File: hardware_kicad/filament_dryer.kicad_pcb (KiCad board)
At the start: 2 copper layers, 94 x 130 mm, 98 parts, among them J1 USB_C_Receptacle_USB2.0, J2 H/T Ambient, J3 T Aux, J4 Peristaltic Pump, Q1 NMOS, Q2 NMOS, Q3 NMOS, Q4 NMOS, U1 W25Q128JVS, U2 AMS1117-3.3, U3 RP2040, U4 DS18B20Z, U5 H/T Filament, X1 12MHz Yangxing Tech X322512MS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

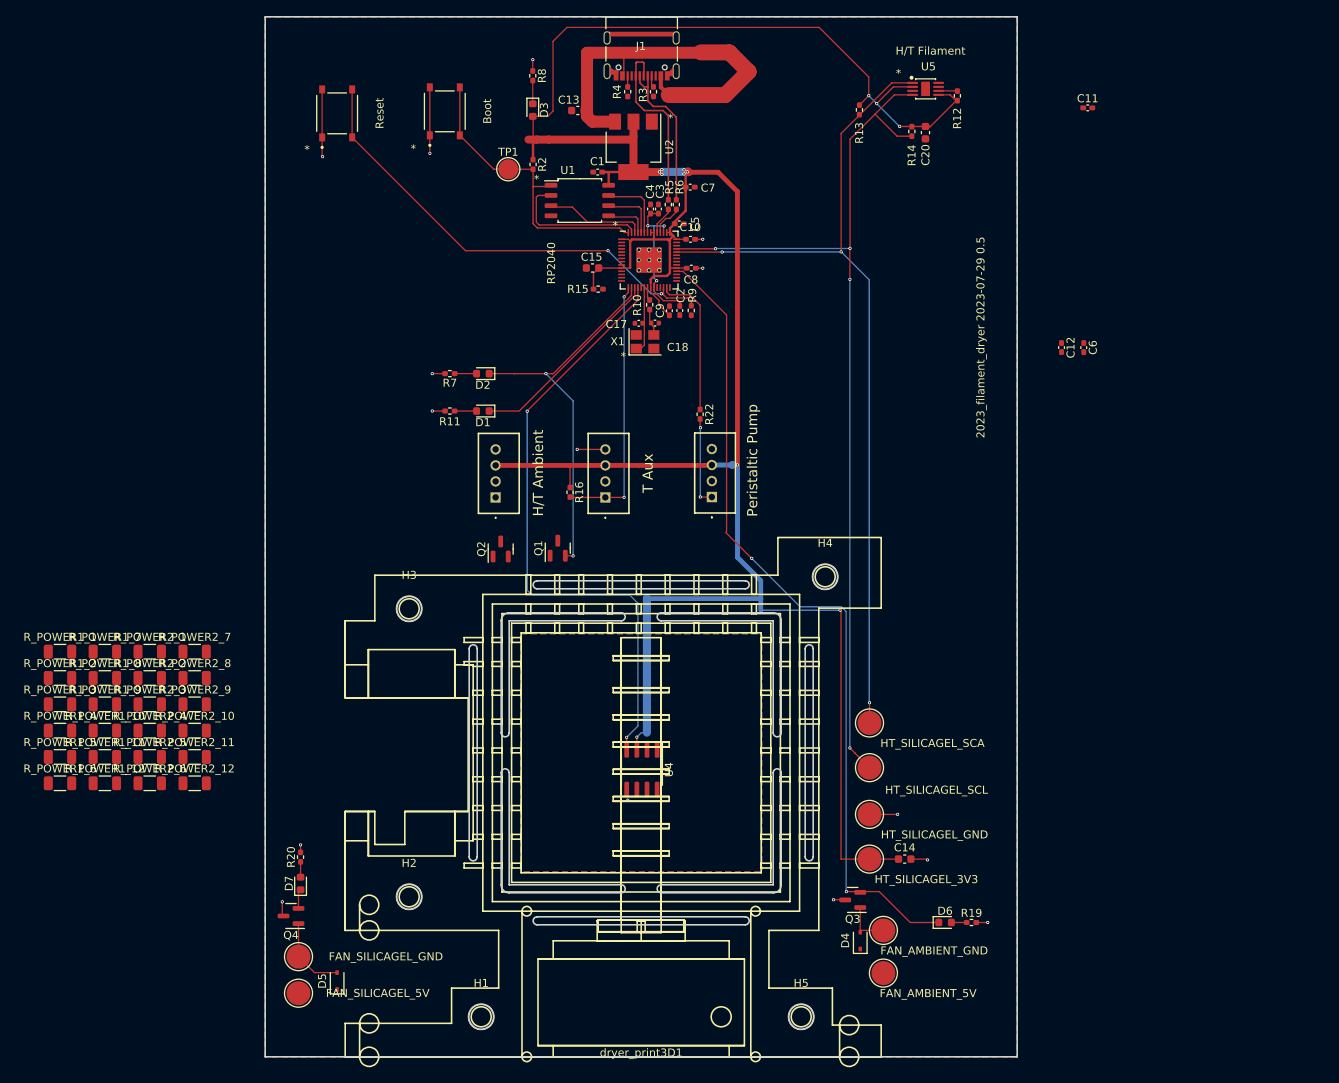
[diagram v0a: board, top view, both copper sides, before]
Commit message: Last version with resistors
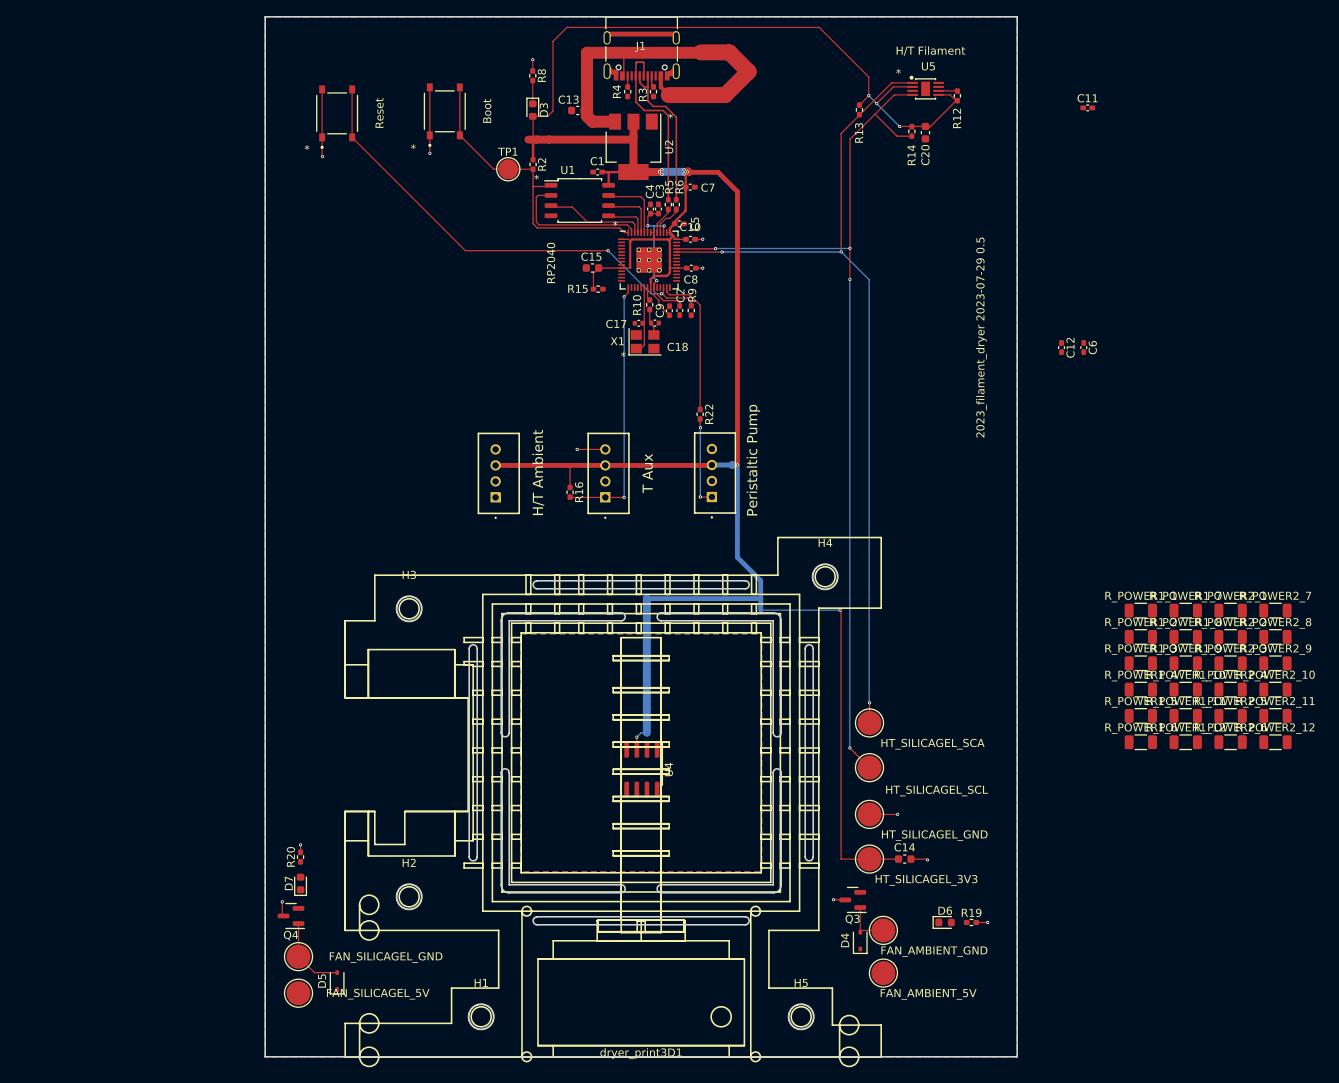
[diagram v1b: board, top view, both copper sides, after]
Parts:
- removed D1: HEATER_2, LED_SMD:LED_0603_1608Metric
- removed D2: HEATER_1, LED_SMD:LED_0603_1608Metric
- removed Q1, Q2: NMOS, Package_TO_SOT_SMD:SOT-23
- removed R11, R7: 470R, Resistor_SMD:R_0402_1005Metric_Pad0.72x0.64mm_HandSolder
- moved R_POWER1_1 135.2 mm to (163.5, 114.2)
- moved R_POWER1_10 135.2 mm to (169.1, 124.1)
- moved R_POWER1_11 135.2 mm to (169.1, 127.4)
- moved R_POWER1_12 135.2 mm to (169.1, 130.7)
- moved R_POWER1_2 135.2 mm to (163.5, 117.5)
- moved R_POWER1_3 135.2 mm to (163.5, 120.8)
- moved R_POWER1_4 135.2 mm to (163.5, 124.1)
- moved R_POWER1_5 135.2 mm to (163.5, 127.4)
- moved R_POWER1_6 135.2 mm to (163.5, 130.7)
- moved R_POWER1_7 135.2 mm to (169.1, 114.2)
- moved R_POWER1_8 135.2 mm to (169.1, 117.5)
- moved R_POWER1_9 135.2 mm to (169.1, 120.8)
- moved R_POWER2_1 135.2 mm to (174.7, 114.2)
- moved R_POWER2_10 135.2 mm to (180.3, 124.1)
- moved R_POWER2_11 135.2 mm to (180.3, 127.4)
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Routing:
- net /GPIO_FAN_AMBIENT: track 104.9 -> 0.00 mm, vias 2 -> 0
- net /T_HEATING_1WIRE: track 77.0 -> 0.00 mm, vias 2 -> 0
- net /GPIO_HEATER_1: track 48.0 -> 0.00 mm, vias 2 -> 0
- net /GPIO_HEATER_2: track 25.1 -> 0.00 mm
- net +5V: track 54.6 -> 49.1 mm
- net /GPIO_FAN_SILICAGEL: track 3.99 -> 0.00 mm
- net Net-(Q2-D): track 1.60 -> 0.00 mm, vias 1 -> 0
- net Net-(Q1-D): track 1.60 -> 0.00 mm, vias 1 -> 0
- net GND: vias 13 -> 12

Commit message: Ready for second review
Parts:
- removed R_POWER1_1, R_POWER1_10, R_POWER1_11, R_POWER1_12, R_POWER1_2, R_POWER1_3, R_POWER1_4, R_POWER1_5, R_POWER1_6, R_POWER1_7, R_POWER1_8, R_POWER1_9, R_POWER2_1, R_POWER2_10, R_POWER2_11, R_POWER2_12, R_POWER2_2, R_POWER2_3, R_POWER2_4, R_POWER2_5, R_POWER2_6, R_POWER2_7, R_POWER2_8, R_POWER2_9: 120, Resistor_SMD:R_1206_3216Metric
- added D10: 1N4148WS, Diode_SMD:D_SOD-323, F.Cu at (84.7, 83.6)
- added D11: 1N4148WS, Diode_SMD:D_SOD-323, F.Cu at (62.7, 83.6)
- added D8: 1N4148WS, Diode_SMD:D_SOD-323, F.Cu at (75.2, 83.6)
- added D9: 1N4148WS, Diode_SMD:D_SOD-323, F.Cu at (136.9, 83.6)
- added JP1: SolderJumper_2_Open, Jumper:SolderJumper-2_P1.3mm_Open_RoundedPad1.0x1.5mm, F.Cu at (70.4, 81.1)
- added JP2: SolderJumper_2_Open, Jumper:SolderJumper-2_P1.3mm_Open_RoundedPad1.0x1.5mm, F.Cu at (132.0, 81.0)
- added JP3: SolderJumper_2_Open, Jumper:SolderJumper-2_P1.3mm_Open_RoundedPad1.0x1.5mm, F.Cu at (79.8, 81.1)
- added JP4: SolderJumper_2_Open, Jumper:SolderJumper-2_P1.3mm_Open_RoundedPad1.0x1.5mm, F.Cu at (57.8, 81.1)
- added NeoC1: 100n, Capacitor_SMD:C_0402_1005Metric_Pad0.74x0.62mm_HandSolder, F.Cu at (87.6, 119.5)
- added NeoC10: 100n, Capacitor_SMD:C_0402_1005Metric_Pad0.74x0.62mm_HandSolder, F.Cu at (87.6, 145.6)
- added NeoC11: 100n, Capacitor_SMD:C_0402_1005Metric_Pad0.74x0.62mm_HandSolder, F.Cu at (109.6, 119.5)
- added NeoC12: 100n, Capacitor_SMD:C_0402_1005Metric_Pad0.74x0.62mm_HandSolder, F.Cu at (109.6, 122.4)
- added NeoC13: 100n, Capacitor_SMD:C_0402_1005Metric_Pad0.74x0.62mm_HandSolder, F.Cu at (109.6, 125.3)
- added NeoC14: 100n, Capacitor_SMD:C_0402_1005Metric_Pad0.74x0.62mm_HandSolder, F.Cu at (109.6, 128.2)
- added NeoC15: 100n, Capacitor_SMD:C_0402_1005Metric_Pad0.74x0.62mm_HandSolder, F.Cu at (109.6, 131.1)
- added NeoC16: 100n, Capacitor_SMD:C_0402_1005Metric_Pad0.74x0.62mm_HandSolder, F.Cu at (109.6, 134.0)
- added NeoC17: 100n, Capacitor_SMD:C_0402_1005Metric_Pad0.74x0.62mm_HandSolder, F.Cu at (109.6, 136.9)
- added NeoC18: 100n, Capacitor_SMD:C_0402_1005Metric_Pad0.74x0.62mm_HandSolder, F.Cu at (109.6, 139.8)
- added NeoC19: 100n, Capacitor_SMD:C_0402_1005Metric_Pad0.74x0.62mm_HandSolder, F.Cu at (109.6, 142.7)
- added NeoC2: 100n, Capacitor_SMD:C_0402_1005Metric_Pad0.74x0.62mm_HandSolder, F.Cu at (87.6, 122.4)
- added NeoC20: 100n, Capacitor_SMD:C_0402_1005Metric_Pad0.74x0.62mm_HandSolder, F.Cu at (109.6, 145.6)
- added NeoC21: 100n, Capacitor_SMD:C_0402_1005Metric_Pad0.74x0.62mm_HandSolder, F.Cu at (97.6, 121.5)
- added NeoC22: 100n, Capacitor_SMD:C_0402_1005Metric_Pad0.74x0.62mm_HandSolder, F.Cu at (97.6, 124.4)
- added NeoC23: 100n, Capacitor_SMD:C_0402_1005Metric_Pad0.74x0.62mm_HandSolder, F.Cu at (97.6, 127.3)
- added NeoC24: 100n, Capacitor_SMD:C_0402_1005Metric_Pad0.74x0.62mm_HandSolder, F.Cu at (97.6, 140.0)
- added NeoC25: 100n, Capacitor_SMD:C_0402_1005Metric_Pad0.74x0.62mm_HandSolder, F.Cu at (97.6, 142.9)
- added NeoC26: 100n, Capacitor_SMD:C_0402_1005Metric_Pad0.74x0.62mm_HandSolder, F.Cu at (97.6, 145.8)
- added NeoC27: 100n, Capacitor_SMD:C_0402_1005Metric_Pad0.74x0.62mm_HandSolder, F.Cu at (58.2, 90.0)
- added NeoC28: 100n, Capacitor_SMD:C_0402_1005Metric_Pad0.74x0.62mm_HandSolder, F.Cu at (58.2, 94.5)
- added NeoC3: 100n, Capacitor_SMD:C_0402_1005Metric_Pad0.74x0.62mm_HandSolder, F.Cu at (87.6, 125.3)
- added NeoC4: 100n, Capacitor_SMD:C_0402_1005Metric_Pad0.74x0.62mm_HandSolder, F.Cu at (87.6, 128.2)
- added NeoC5: 100n, Capacitor_SMD:C_0402_1005Metric_Pad0.74x0.62mm_HandSolder, F.Cu at (87.6, 131.1)
- added NeoC6: 100n, Capacitor_SMD:C_0402_1005Metric_Pad0.74x0.62mm_HandSolder, F.Cu at (87.6, 134.0)
- added NeoC7: 100n, Capacitor_SMD:C_0402_1005Metric_Pad0.74x0.62mm_HandSolder, F.Cu at (87.6, 136.9)
- added NeoC8: 100n, Capacitor_SMD:C_0402_1005Metric_Pad0.74x0.62mm_HandSolder, F.Cu at (87.6, 139.8)
- added NeoC9: 100n, Capacitor_SMD:C_0402_1005Metric_Pad0.74x0.62mm_HandSolder, F.Cu at (87.6, 142.7)
- added NeoD1: WS2812B-2020, LED_SMD:LED_WS2812B-2020_PLCC4_2.0x2.0mm, F.Cu at (91.0, 119.0)
- added NeoD10: WS2812B-2020, LED_SMD:LED_WS2812B-2020_PLCC4_2.0x2.0mm, F.Cu at (91.0, 145.1)
- added NeoD11: WS2812B-2020, LED_SMD:LED_WS2812B-2020_PLCC4_2.0x2.0mm, F.Cu at (113.0, 119.0)
- added NeoD12: WS2812B-2020, LED_SMD:LED_WS2812B-2020_PLCC4_2.0x2.0mm, F.Cu at (113.0, 121.9)
- added NeoD13: WS2812B-2020, LED_SMD:LED_WS2812B-2020_PLCC4_2.0x2.0mm, F.Cu at (113.0, 124.8)
- added NeoD14: WS2812B-2020, LED_SMD:LED_WS2812B-2020_PLCC4_2.0x2.0mm, F.Cu at (113.0, 127.7)
- added NeoD15: WS2812B-2020, LED_SMD:LED_WS2812B-2020_PLCC4_2.0x2.0mm, F.Cu at (113.0, 130.6)
- added NeoD16: WS2812B-2020, LED_SMD:LED_WS2812B-2020_PLCC4_2.0x2.0mm, F.Cu at (113.0, 133.5)
- added NeoD17: WS2812B-2020, LED_SMD:LED_WS2812B-2020_PLCC4_2.0x2.0mm, F.Cu at (113.0, 136.4)
- added NeoD18: WS2812B-2020, LED_SMD:LED_WS2812B-2020_PLCC4_2.0x2.0mm, F.Cu at (113.0, 139.3)
- added NeoD19: WS2812B-2020, LED_SMD:LED_WS2812B-2020_PLCC4_2.0x2.0mm, F.Cu at (113.0, 142.2)
- added NeoD2: WS2812B-2020, LED_SMD:LED_WS2812B-2020_PLCC4_2.0x2.0mm, F.Cu at (91.0, 121.9)
- added NeoD20: WS2812B-2020, LED_SMD:LED_WS2812B-2020_PLCC4_2.0x2.0mm, F.Cu at (113.0, 145.1)
- added NeoD21: WS2812B-2020, LED_SMD:LED_WS2812B-2020_PLCC4_2.0x2.0mm, F.Cu at (101.0, 121.0)
- added NeoD22: WS2812B-2020, LED_SMD:LED_WS2812B-2020_PLCC4_2.0x2.0mm, F.Cu at (101.0, 123.9)
- added NeoD23: WS2812B-2020, LED_SMD:LED_WS2812B-2020_PLCC4_2.0x2.0mm, F.Cu at (101.0, 126.8)
- added NeoD24: WS2812B-2020, LED_SMD:LED_WS2812B-2020_PLCC4_2.0x2.0mm, F.Cu at (101.0, 139.5)
- added NeoD25: WS2812B-2020, LED_SMD:LED_WS2812B-2020_PLCC4_2.0x2.0mm, F.Cu at (101.0, 142.4)
- added NeoD26: WS2812B-2020, LED_SMD:LED_WS2812B-2020_PLCC4_2.0x2.0mm, F.Cu at (101.0, 145.3)
- added NeoD27: WS2812B-2020, LED_SMD:LED_WS2812B-2020_PLCC4_2.0x2.0mm, F.Cu at (61.6, 89.4)
- added NeoD28: WS2812B-2020, LED_SMD:LED_WS2812B-2020_PLCC4_2.0x2.0mm, F.Cu at (61.8, 94.0)
- added NeoD3: WS2812B-2020, LED_SMD:LED_WS2812B-2020_PLCC4_2.0x2.0mm, F.Cu at (91.0, 124.8)
- added NeoD4: WS2812B-2020, LED_SMD:LED_WS2812B-2020_PLCC4_2.0x2.0mm, F.Cu at (91.0, 127.7)
- added NeoD5: WS2812B-2020, LED_SMD:LED_WS2812B-2020_PLCC4_2.0x2.0mm, F.Cu at (91.0, 130.6)
- added NeoD6: WS2812B-2020, LED_SMD:LED_WS2812B-2020_PLCC4_2.0x2.0mm, F.Cu at (91.0, 133.5)
- added NeoD7: WS2812B-2020, LED_SMD:LED_WS2812B-2020_PLCC4_2.0x2.0mm, F.Cu at (91.0, 136.4)
- added NeoD8: WS2812B-2020, LED_SMD:LED_WS2812B-2020_PLCC4_2.0x2.0mm, F.Cu at (91.0, 139.3)
- added NeoD9: WS2812B-2020, LED_SMD:LED_WS2812B-2020_PLCC4_2.0x2.0mm, F.Cu at (91.0, 142.2)
- added Q5: NMOS, Package_TO_SOT_SMD:SOT-23, F.Cu at (75.3, 78.8)
- added Q6: NMOS, Package_TO_SOT_SMD:SOT-23, F.Cu at (136.7, 77.9)
- added Q7: NMOS, Package_TO_SOT_SMD:SOT-23, F.Cu at (84.7, 78.8)
- added Q8: NMOS, Package_TO_SOT_SMD:SOT-23, F.Cu at (62.6, 78.8)
- added R1: 4K7, Resistor_SMD:R_0402_1005Metric_Pad0.72x0.64mm_HandSolder, F.Cu at (85.8, 117.9)
- added R17: 4K7, Resistor_SMD:R_0402_1005Metric_Pad0.72x0.64mm_HandSolder, F.Cu at (109.6, 118.5)
- added R18: 4K7, Resistor_SMD:R_0402_1005Metric_Pad0.72x0.64mm_HandSolder, F.Cu at (97.6, 120.4)
- added R21: 4K7, Resistor_SMD:R_0402_1005Metric_Pad0.72x0.64mm_HandSolder, F.Cu at (58.2, 88.9)
- moved C11 62.0 mm to (96.9, 67.1), turned to 180 degrees
- moved C6 52.1 mm to (107.1, 64.5), turned to 0 degrees
- moved C12 48.1 mm to (105.6, 76.7)
- moved R9 16.5 mm to (93.8, 67.1), turned to 180 degrees
- moved C2 1.04 mm to (106.9, 76.7)
- moved U4 0.16 mm to (101.0, 134.2), turned to 0 degrees
- moved D6 0.11 mm to (138.9, 153.2), turned to 180 degrees
- turned C9 to -90 degrees
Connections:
- U3 pad 12: /T_BOARD_1WIRE -> unconnected-(U3-GPIO9-Pad12)
- U3 pad 2: /T_BOARD_1WIRE -> /GPIO_NP_BOARD
- U3 pad 3: unconnected-(U3-GPIO1-Pad3) -> /GPIO_NP_A
- U3 pad 37: unconnected-(U3-GPIO25-Pad37) -> /GPIO_NP_B
- U3 pad 4: unconnected-(U3-GPIO2-Pad4) -> /GPIO_NP_C
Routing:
- net +5V: track 49.1 -> 294.9 mm, vias 0 -> 2
- net GND: track 45.7 -> 185.0 mm, vias 12 -> 108
- net /GPIO_FAN_AMBIENT: track 0.00 -> 107.6 mm, vias 0 -> 4
- net /T_HEATING_1WIRE: track 0.00 -> 90.0 mm, vias 0 -> 3
- net Net-(D9-K): track 0.00 -> 85.7 mm
- net +3V3: track 339.4 -> 424.0 mm, vias 12 -> 14
- net Net-(D8-K): track 0.00 -> 73.2 mm
- net Net-(D10-K): track 0.00 -> 60.4 mm
- net /GPIO_NP_BOARD: track 0.00 -> 48.2 mm
- net /GPIO_NP_B: track 0.00 -> 35.8 mm, vias 0 -> 2
- net /GPIO_NP_A: track 0.00 -> 35.4 mm
- net /GPIO_NP_C: track 0.00 -> 27.0 mm
- net Net-(D11-K): track 0.00 -> 12.4 mm
- net Net-(NeoD23-DOUT): track 0.00 -> 12.3 mm
- net Net-(D9-A): track 0.00 -> 4.71 mm
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- added copper zone on F.Cu, net +5V

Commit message: After second review
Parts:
- removed D10, D11, D4, D5, D8, D9: 1N4148WS, Diode_SMD:D_SOD-323
- added D1: General Purpose Diode, Diode_SMD:D_SMA, F.Cu at (127.3, 157.0)
- added D2: General Purpose Diode, Diode_SMD:D_SMA, F.Cu at (64.3, 159.5)
- moved D7 2.10 mm to (60.5, 148.7), turned to -90 degrees
- moved R20 2.09 mm to (60.5, 145.3)
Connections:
- JP1 pad 2: Net-(D8-A) -> Net-(JP1-B)
- JP2 pad 2: Net-(D9-A) -> Net-(JP2-B)
- JP3 pad 2: Net-(D10-A) -> Net-(JP3-B)
- JP4 pad 2: Net-(D11-A) -> Net-(JP4-B)
- NeoC28 pad 2: unconnected-(NeoC28-Pad2) -> GND
- NeoD1 pad 3: Net-(D8-K) -> Net-(JP1-B)
- NeoD11 pad 3: Net-(D9-K) -> Net-(JP2-B)
- NeoD21 pad 3: Net-(D10-K) -> Net-(JP3-B)
- NeoD27 pad 3: Net-(D11-K) -> Net-(JP4-B)
- Q5 pad 1: Net-(D8-K) -> Net-(JP1-B)
- Q6 pad 1: Net-(D9-K) -> Net-(JP2-B)
- Q7 pad 1: Net-(D10-K) -> Net-(JP3-B)
- Q8 pad 1: Net-(D11-K) -> Net-(JP4-B)
- R1 pad 2: Net-(D8-K) -> Net-(JP1-B)
- R17 pad 2: Net-(D9-K) -> Net-(JP2-B)
- R18 pad 2: Net-(D10-K) -> Net-(JP3-B)
- R21 pad 2: Net-(D11-K) -> Net-(JP4-B)
- U3 pad 12: unconnected-(U3-GPIO9-Pad12) -> /GPIO_FAN_SILICAGEL
- U3 pad 13: /HT_GROVE_SDA -> unconnected-(U3-GPIO10-Pad13)
- U3 pad 14: /HT_GROVE_SCL -> unconnected-(U3-GPIO11-Pad14)
- U3 pad 15: /T_AUX_1WIRE -> /HT_GROVE_SDA
- U3 pad 16: /GPIO_HEATER_1 -> /HT_GROVE_SCL
- U3 pad 17: /GPIO_HEATER_2 -> /T_AUX_1WIRE
- U3 pad 6: /HT_GROVE_SDA -> unconnected-(U3-GPIO4-Pad6)
- U3 pad 7: /HT_GROVE_SCL -> unconnected-(U3-GPIO5-Pad7)
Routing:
- net /GPIO_FAN_SILICAGEL: track 0.00 -> 99.2 mm, vias 0 -> 2
- net Net-(JP2-B): track 0.00 -> 91.1 mm
- net Net-(D9-K): track 85.7 -> 0.00 mm
- net Net-(JP1-B): track 0.00 -> 79.2 mm
- net Net-(D8-K): track 73.2 -> 0.00 mm
- net Net-(JP3-B): track 0.00 -> 64.4 mm
- net Net-(D10-K): track 60.4 -> 0.00 mm
- net /HT_GROVE_SCL: track 0.00 -> 35.2 mm, vias 0 -> 2
- net /HT_GROVE_SDA: track 0.00 -> 32.3 mm
- net Net-(JP4-B): track 0.00 -> 18.0 mm
- net Net-(D11-K): track 12.4 -> 0.00 mm
- net Net-(D9-A): track 4.71 -> 0.00 mm
- net GND: track 185.0 -> 189.7 mm, vias 108 -> 109
- net Net-(D10-A): track 4.63 -> 0.00 mm
- net Net-(D11-A): track 4.62 -> 0.00 mm
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
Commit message: After second review 2
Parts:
- D3, D6, D7: footprint LED_SMD:LED_0603_1608Metric -> 00_project_library:LED_0603_1608Metric
- NeoD1, NeoD10, NeoD11, NeoD12, NeoD13, NeoD14, NeoD15, NeoD16, NeoD17, NeoD18, NeoD19, NeoD2, NeoD20, NeoD21, NeoD22, NeoD23, NeoD24, NeoD25, NeoD26, NeoD27, NeoD28, NeoD3, NeoD4, NeoD5, NeoD6, NeoD7, NeoD8, NeoD9: footprint LED_SMD:LED_WS2812B-2020_PLCC4_2.0x2.0mm -> 00_project_library:LED_WS2812B-2020_PLCC4_2.0x2.0mm
- Q3, Q4, Q5, Q6, Q7, Q8: footprint Package_TO_SOT_SMD:SOT-23 -> 00_project_library:SOT-23
- U1: footprint Package_SO:SOIC-8_5.23x5.23mm_P1.27mm -> 00_project_library:SOIC-8_5.23x5.23mm_P1.27mm
- U4: footprint Package_SO:SOIC-8_3.9x4.9mm_P1.27mm -> 00_project_library:SOIC-8_3.9x4.9mm_P1.27mm
- X1: footprint Crystal:Crystal_SMD_3225-4Pin_3.2x2.5mm -> 00_project_library:Crystal_SMD_3225-4Pin_3.2x2.5mm
- moved Q5 0.51 mm to (74.8, 78.8), turned to 0 degrees
- moved Q3 0.50 mm to (126.9, 150.4), turned to 0 degrees
- moved Q4 0.50 mm to (56.7, 152.4), turned to 0 degrees
- moved Q7 0.41 mm to (84.3, 78.8), turned to 0 degrees
- moved Q6 0.40 mm to (136.3, 77.9), turned to 0 degrees
- moved Q8 0.38 mm to (62.2, 78.8), turned to 0 degrees
- turned U1 to -90 degrees
- turned U2 to 90 degrees
- turned U4 to -90 degrees
- turned U5 to -90 degrees
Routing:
- net +5V: track 291.9 -> 294.0 mm

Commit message: hardware_kicad v0.6
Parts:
- D1, D2: footprint Diode_SMD:D_SMA -> 00_project_library:D_SMA
- NeoD1, NeoD10, NeoD11, NeoD12, NeoD13, NeoD14, NeoD15, NeoD16, NeoD17, NeoD18, NeoD19, NeoD2, NeoD20, NeoD21, NeoD22, NeoD23, NeoD24, NeoD25, NeoD26, NeoD27, NeoD28, NeoD3, NeoD4, NeoD5, NeoD6, NeoD7, NeoD8, NeoD9: footprint 00_project_library:LED_WS2812B-2020_PLCC4_2.0x2.0mm -> LED_SMD:LED_WS2812B-2020_PLCC4_2.0x2.0mm
- U2: footprint Package_TO_SOT_SMD:SOT-223-3_TabPin2 -> 00_project_library:SOT-223-3_TabPin2
- moved TP7 0.99 mm to (132.2, 159.3)
- moved TP8 0.97 mm to (132.2, 154.2)
- moved U2 0.12 mm to (100.1, 56.2)
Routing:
- net Net-(D1-A): track 6.05 -> 7.02 mm
- net +5V: track 294.0 -> 295.0 mm
